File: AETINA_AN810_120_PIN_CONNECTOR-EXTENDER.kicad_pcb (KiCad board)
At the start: 2 copper layers, 86.5 x 20 mm, 4 parts, among them J1 QTH-060-01-X-D-A, J2 QSH-060-01-X-D-A

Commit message: Routing completed
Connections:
- J1 pad 01: Net-(J1-Pad01) -> /DSI3_D1_N
- J1 pad 02: Net-(J1-Pad02) -> /VDD_SYS_BL
- J1 pad 03: Net-(J1-Pad03) -> /DSI3_D1_P
- J1 pad 04: Net-(J1-Pad04) -> /VDD_SYS_BL
- J1 pad 05: Net-(J1-Pad05) -> GND
- J1 pad 06: Net-(J1-Pad06) -> /VDD_SYS_BL
- J1 pad 07: Net-(J1-Pad07) -> /DSI3_D0_N
- J1 pad 08: Net-(J1-Pad08) -> /LCD_BKLT_EN
- J1 pad 09: Net-(J1-Pad09) -> /DSI3_D0_P
- J1 pad 10: Net-(J1-Pad10) -> /LCD_BKLT0_PWM
- J1 pad 100: (no net) -> /LCD_BKLT1_PWM
- J1 pad 101: (no net) -> /DP0_TX1_N
- J1 pad 102: (no net) -> GND
- J1 pad 103: (no net) -> GND
- J1 pad 104: (no net) -> /SPI2_SCK
- J1 pad 105: (no net) -> /DP0_TX2_P
- J1 pad 106: (no net) -> /SPI2_MISO
- J1 pad 107: (no net) -> /DP0_TX2_N
- J1 pad 108: (no net) -> /SPI2_MOSI
- J1 pad 109: (no net) -> GND
- J1 pad 11: Net-(J1-Pad11) -> GND
- J1 pad 110: (no net) -> /SPI2_CS0
- J1 pad 111: (no net) -> Net-(J1-Pad111)
- J1 pad 112: (no net) -> GND
- J1 pad 113: (no net) -> Net-(J1-Pad113)
- J1 pad 114: (no net) -> Net-(J1-Pad114)
- J1 pad 115: (no net) -> GND
- J1 pad 116: (no net) -> Net-(J1-Pad116)
- J1 pad 117: (no net) -> /DP0_TX3_P
- J1 pad 118: (no net) -> Net-(J1-Pad118)
- J1 pad 119: (no net) -> /DP0_TX3_N
- J1 pad 12: Net-(J1-Pad12) -> /LCD_EN
- J1 pad 120: (no net) -> Net-(J1-Pad120)
- J1 pad 13: Net-(J1-Pad13) -> /DSI3_CLK_N
- J1 pad 14: Net-(J1-Pad14) -> /LCD_TE
- J1 pad 15: Net-(J1-Pad15) -> /DSI3_CLK_P
- J1 pad 16: Net-(J1-Pad16) -> /VDD_3V3_SLP
- J1 pad 17: Net-(J1-Pad17) -> GND
- J1 pad 18: Net-(J1-Pad18) -> /BRIDGE_EN
- J1 pad 19: Net-(J1-Pad19) -> /DSI2_D1_N
- J1 pad 20: Net-(J1-Pad20) -> /BRIDGE_IRQ
- J1 pad 21: Net-(J1-Pad21) -> /DSI2_D1_P
- J1 pad 22: Net-(J1-Pad22) -> /I2C_GP0_CLK
- J1 pad 23: Net-(J1-Pad23) -> GND
- J1 pad 24: Net-(J1-Pad24) -> /I2C_GP0_DAT
- J1 pad 25: Net-(J1-Pad25) -> /DSI2_D0_N
- J1 pad 26: Net-(J1-Pad26) -> /AVDD_TS_DIS
- J1 pad 27: Net-(J1-Pad27) -> /DSI2_D0_P
- J1 pad 28: Net-(J1-Pad28) -> /VDD_TS_1V8
- J1 pad 29: Net-(J1-Pad29) -> GND
- J1 pad 30: Net-(J1-Pad30) -> /I2C_GP1_CLK
- J1 pad 31: Net-(J1-Pad31) -> /DSI1_D1_N
- J1 pad 32: Net-(J1-Pad32) -> /I2C_GP1_DAT
- J1 pad 33: Net-(J1-Pad33) -> /DSI1_D1_P
- J1 pad 35: Net-(J1-Pad35) -> GND
- J1 pad 37: Net-(J1-Pad37) -> /DSI1_D0_N
- J1 pad 39: Net-(J1-Pad39) -> /DSI1_D0_P
- J1 pad 41: Net-(J1-Pad41) -> GND
- J1 pad 43: Net-(J1-Pad43) -> /DSI0_CLK_N
- J1 pad 45: Net-(J1-Pad45) -> /DSI0_CLK_P
- J1 pad 47: Net-(J1-Pad47) -> GND
- J1 pad 48: Net-(J1-Pad48) -> GND
- J1 pad 49: Net-(J1-Pad49) -> /DSI0_D1_N
- J1 pad 51: Net-(J1-Pad51) -> /DSI0_D1_P
- J1 pad 52: Net-(J1-Pad52) -> GND
- J1 pad 53: Net-(J1-Pad53) -> GND
- J1 pad 54: Net-(J1-Pad54) -> /VDD_DIS_3V3_LCD
- J1 pad 55: Net-(J1-Pad55) -> /DSI0_D0_N
- J1 pad 56: Net-(J1-Pad56) -> /VDD_DIS_3V3_LCD
- J1 pad 57: Net-(J1-Pad57) -> /DSI0_D0_P
- J1 pad 58: Net-(J1-Pad58) -> /VDD_LCD_1V8_DIS
- J1 pad 59: Net-(J1-Pad59) -> GND
- J1 pad 60: Net-(J1-Pad60) -> GND
- J1 pad 61: (no net) -> /VDD_3V3_SYS
- J1 pad 62: (no net) -> /LCD_VDD_EN
- J1 pad 63: (no net) -> /VDD_3V3_SYS
- J1 pad 64: (no net) -> Net-(J1-Pad64)
- J1 pad 65: (no net) -> GND
- J1 pad 66: (no net) -> /DSI1_CLK_P
- J1 pad 67: (no net) -> GND
- J1 pad 68: (no net) -> /DSI1_CLK_N
- J1 pad 69: (no net) -> /VDD_1V8
- J1 pad 70: (no net) -> GND
- J1 pad 71: (no net) -> /VDD_1V8
- J1 pad 72: (no net) -> /DSI2_CLK_P
- J1 pad 73: (no net) -> GND
- J1 pad 74: (no net) -> /DSI2_CLK_N
- J1 pad 75: (no net) -> GND
- J1 pad 76: (no net) -> GND
- J1 pad 77: (no net) -> /VDD_1V2
- J1 pad 78: (no net) -> GND
- J1 pad 79: (no net) -> /VDD_1V2
- J1 pad 80: (no net) -> /VDD_5V0_IO_SYS
- J1 pad 81: (no net) -> GND
- J1 pad 82: (no net) -> Net-(J1-Pad82)
- J1 pad 83: (no net) -> GND
- J1 pad 84: (no net) -> Net-(J1-Pad84)
- J1 pad 85: (no net) -> /DP_HPD
- J1 pad 86: (no net) -> /CHARGER_PRSNT
- J1 pad 87: (no net) -> /DP0_AUX_CH_N
- J1 pad 88: (no net) -> /LCD_BIAS_EN
- J1 pad 89: (no net) -> /DP0_AUX_CH_P
- J1 pad 90: (no net) -> GND
- J1 pad 91: (no net) -> GND
- J1 pad 92: (no net) -> /GSYNC_VSYNC
- J1 pad 93: (no net) -> /DP0_TX0_P
- J1 pad 94: (no net) -> /GSYNC_HSYNC
- J1 pad 95: (no net) -> /DP0_TX0_N
- J1 pad 96: (no net) -> GND
- J1 pad 97: (no net) -> GND
- J1 pad 98: (no net) -> /NVSR_INT
- J1 pad 99: (no net) -> /DP0_TX1_P
- J1 pad G1: Net-(J1-PadG1) -> GND
- J1 pad G2: Net-(J1-PadG1) -> GND
- J1 pad G3: Net-(J1-PadG1) -> GND
- J1 pad G4: Net-(J1-PadG1) -> GND
- J1 pad G5: Net-(J1-PadG1) -> GND
- J1 pad G6: Net-(J1-PadG1) -> GND
- J1 pad G7: Net-(J1-PadG1) -> GND
- J1 pad G8: Net-(J1-PadG1) -> GND
- J2 pad 01: Net-(J2-Pad01) -> /DSI3_D1_N
- J2 pad 02: Net-(J2-Pad02) -> /VDD_SYS_BL
- J2 pad 03: Net-(J2-Pad03) -> /DSI3_D1_P
- J2 pad 04: Net-(J2-Pad04) -> /VDD_SYS_BL
- J2 pad 05: Net-(J2-Pad05) -> GND
- J2 pad 06: Net-(J2-Pad06) -> /VDD_SYS_BL
- J2 pad 07: Net-(J2-Pad07) -> /DSI3_D0_N
- J2 pad 08: Net-(J2-Pad08) -> /LCD_BKLT_EN
- J2 pad 09: Net-(J2-Pad09) -> /DSI3_D0_P
- J2 pad 10: Net-(J2-Pad10) -> /LCD_BKLT0_PWM
- J2 pad 100: (no net) -> /LCD_BKLT1_PWM
- J2 pad 101: (no net) -> /DP0_TX1_N
- J2 pad 102: (no net) -> GND
- J2 pad 103: (no net) -> GND
- J2 pad 104: (no net) -> /SPI2_SCK
- J2 pad 105: (no net) -> /DP0_TX2_P
- J2 pad 106: (no net) -> /SPI2_MISO
- J2 pad 107: (no net) -> /DP0_TX2_N
- J2 pad 108: (no net) -> /SPI2_MOSI
- J2 pad 109: (no net) -> GND
- J2 pad 11: Net-(J2-Pad11) -> GND
- J2 pad 110: (no net) -> /SPI2_CS0
- J2 pad 111: (no net) -> Net-(J2-Pad111)
- J2 pad 112: (no net) -> GND
- J2 pad 113: (no net) -> Net-(J2-Pad113)
- J2 pad 114: (no net) -> Net-(J2-Pad114)
- J2 pad 115: (no net) -> GND
- J2 pad 116: (no net) -> Net-(J2-Pad116)
- J2 pad 117: (no net) -> /DP0_TX3_P
- J2 pad 118: (no net) -> Net-(J2-Pad118)
- J2 pad 119: (no net) -> /DP0_TX3_N
- J2 pad 12: Net-(J2-Pad12) -> /LCD_EN
- J2 pad 120: (no net) -> Net-(J2-Pad120)
- J2 pad 13: Net-(J2-Pad13) -> /DSI3_CLK_N
- J2 pad 14: Net-(J2-Pad14) -> /LCD_TE
- J2 pad 15: Net-(J2-Pad15) -> /DSI3_CLK_P
- J2 pad 16: Net-(J2-Pad16) -> /VDD_3V3_SLP
- J2 pad 17: Net-(J2-Pad17) -> GND
- J2 pad 18: Net-(J2-Pad18) -> /BRIDGE_EN
- J2 pad 19: Net-(J2-Pad19) -> /DSI2_D1_N
- J2 pad 20: Net-(J2-Pad20) -> /BRIDGE_IRQ
- J2 pad 21: Net-(J2-Pad21) -> /DSI2_D1_P
- J2 pad 22: Net-(J2-Pad22) -> /I2C_GP0_CLK
- J2 pad 23: Net-(J2-Pad23) -> GND
- J2 pad 24: Net-(J2-Pad24) -> /I2C_GP0_DAT
- J2 pad 25: Net-(J2-Pad25) -> /DSI2_D0_N
- J2 pad 26: Net-(J2-Pad26) -> /AVDD_TS_DIS
- J2 pad 27: Net-(J2-Pad27) -> /DSI2_D0_P
- J2 pad 28: Net-(J2-Pad28) -> /VDD_TS_1V8
- J2 pad 29: Net-(J2-Pad29) -> GND
- J2 pad 30: Net-(J2-Pad30) -> /I2C_GP1_CLK
- J2 pad 31: Net-(J2-Pad31) -> /DSI1_D1_N
- J2 pad 32: Net-(J2-Pad32) -> /I2C_GP1_DAT
- J2 pad 33: Net-(J2-Pad33) -> /DSI1_D1_P
- J2 pad 35: Net-(J2-Pad35) -> GND
- J2 pad 37: Net-(J2-Pad37) -> /DSI1_D0_N
- J2 pad 39: Net-(J2-Pad39) -> /DSI1_D0_P
- J2 pad 41: Net-(J2-Pad41) -> GND
- J2 pad 43: Net-(J2-Pad43) -> /DSI0_CLK_N
- J2 pad 45: Net-(J2-Pad45) -> /DSI0_CLK_P
- J2 pad 47: Net-(J2-Pad47) -> GND
- J2 pad 48: Net-(J2-Pad48) -> GND
- J2 pad 49: Net-(J2-Pad49) -> /DSI0_D1_N
- J2 pad 51: Net-(J2-Pad51) -> /DSI0_D1_P
- J2 pad 52: Net-(J2-Pad52) -> GND
- J2 pad 53: Net-(J2-Pad53) -> GND
- J2 pad 54: Net-(J2-Pad54) -> /VDD_DIS_3V3_LCD
- J2 pad 55: Net-(J2-Pad55) -> /DSI0_D0_N
- J2 pad 56: Net-(J2-Pad56) -> /VDD_DIS_3V3_LCD
- J2 pad 57: Net-(J2-Pad57) -> /DSI0_D0_P
- J2 pad 58: Net-(J2-Pad58) -> /VDD_LCD_1V8_DIS
- J2 pad 59: Net-(J2-Pad59) -> GND
- J2 pad 60: Net-(J2-Pad60) -> GND
- J2 pad 61: (no net) -> /VDD_3V3_SYS
- J2 pad 62: (no net) -> /LCD_VDD_EN
- J2 pad 63: (no net) -> /VDD_3V3_SYS
- J2 pad 64: (no net) -> Net-(J2-Pad64)
- J2 pad 65: (no net) -> GND
- J2 pad 66: (no net) -> /DSI1_CLK_P
- J2 pad 67: (no net) -> GND
- J2 pad 68: (no net) -> /DSI1_CLK_N
- J2 pad 69: (no net) -> /VDD_1V8
- J2 pad 70: (no net) -> GND
- J2 pad 71: (no net) -> /VDD_1V8
- J2 pad 72: (no net) -> /DSI2_CLK_P
- J2 pad 73: (no net) -> GND
- J2 pad 74: (no net) -> /DSI2_CLK_N
- J2 pad 75: (no net) -> GND
- J2 pad 76: (no net) -> GND
- J2 pad 77: (no net) -> /VDD_1V2
- J2 pad 78: (no net) -> GND
- J2 pad 79: (no net) -> /VDD_1V2
- J2 pad 80: (no net) -> /VDD_5V0_IO_SYS
- J2 pad 81: (no net) -> GND
- J2 pad 82: (no net) -> Net-(J2-Pad82)
- J2 pad 83: (no net) -> GND
- J2 pad 84: (no net) -> Net-(J2-Pad84)
- J2 pad 85: (no net) -> /DP_HPD
- J2 pad 86: (no net) -> /CHARGER_PRSNT
- J2 pad 87: (no net) -> /DP0_AUX_CH_N
- J2 pad 88: (no net) -> /LCD_BIAS_EN
- J2 pad 89: (no net) -> /DP0_AUX_CH_P
- J2 pad 90: (no net) -> GND
- J2 pad 91: (no net) -> GND
- J2 pad 92: (no net) -> /GSYNC_VSYNC
- J2 pad 93: (no net) -> /DP0_TX0_P
- J2 pad 94: (no net) -> /GSYNC_HSYNC
- J2 pad 95: (no net) -> /DP0_TX0_N
- J2 pad 96: (no net) -> GND
- J2 pad 97: (no net) -> GND
- J2 pad 98: (no net) -> /NVSR_INT
- J2 pad 99: (no net) -> /DP0_TX1_P
- J2 pad G1_1: Net-(J2-PadG1_1) -> GND
- J2 pad G1_2: Net-(J2-PadG1_1) -> GND
- J2 pad G1_3: Net-(J2-PadG1_1) -> GND
- J2 pad G1_4: Net-(J2-PadG1_1) -> GND
- J2 pad G2_1: (no net) -> GND
- J2 pad G2_2: (no net) -> GND
- J2 pad G2_3: (no net) -> GND
- J2 pad G2_4: (no net) -> GND
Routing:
- net GND: track 0.00 -> 259.3 mm, vias 0 -> 11
- net /VDD_SYS_BL: track 0.00 -> 21.4 mm, vias 0 -> 1
- net /VDD_1V2: track 0.00 -> 16.1 mm, vias 0 -> 1
- net /VDD_1V8: track 0.00 -> 15.7 mm, vias 0 -> 1
- net /I2C_GP1_DAT: track 0.00 -> 15.6 mm, vias 0 -> 1
- net /VDD_DIS_3V3_LCD: track 0.00 -> 15.5 mm, vias 0 -> 1
- net /VDD_3V3_SYS: track 0.00 -> 15.3 mm, vias 0 -> 1
- net /I2C_GP1_CLK: track 0.00 -> 15.2 mm, vias 0 -> 1
- net /DSI0_D0_P: track 0.00 -> 14.9 mm, vias 0 -> 1
- net /DSI0_D0_N: track 0.00 -> 14.4 mm, vias 0 -> 1
- net /DSI0_D1_P: track 0.00 -> 13.7 mm, vias 0 -> 1
- net /VDD_TS_1V8: track 0.00 -> 13.6 mm, vias 0 -> 1
- net /DSI0_CLK_P: track 0.00 -> 13.0 mm, vias 0 -> 1
- net /DSI0_D1_N: track 0.00 -> 13.0 mm, vias 0 -> 1
- net /DSI1_D0_P: track 0.00 -> 12.6 mm, vias 0 -> 1
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- added copper zone on B.Cu, net GND
- added copper zone on F.Cu, net GND

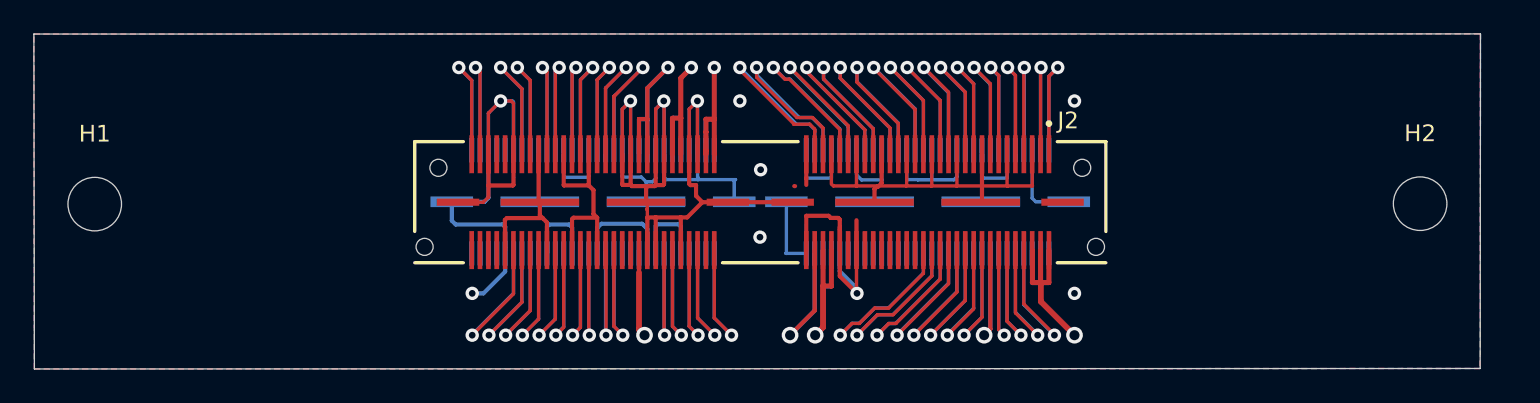
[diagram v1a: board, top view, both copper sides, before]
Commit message: Fix wrong wiring by referring to incorrect connector
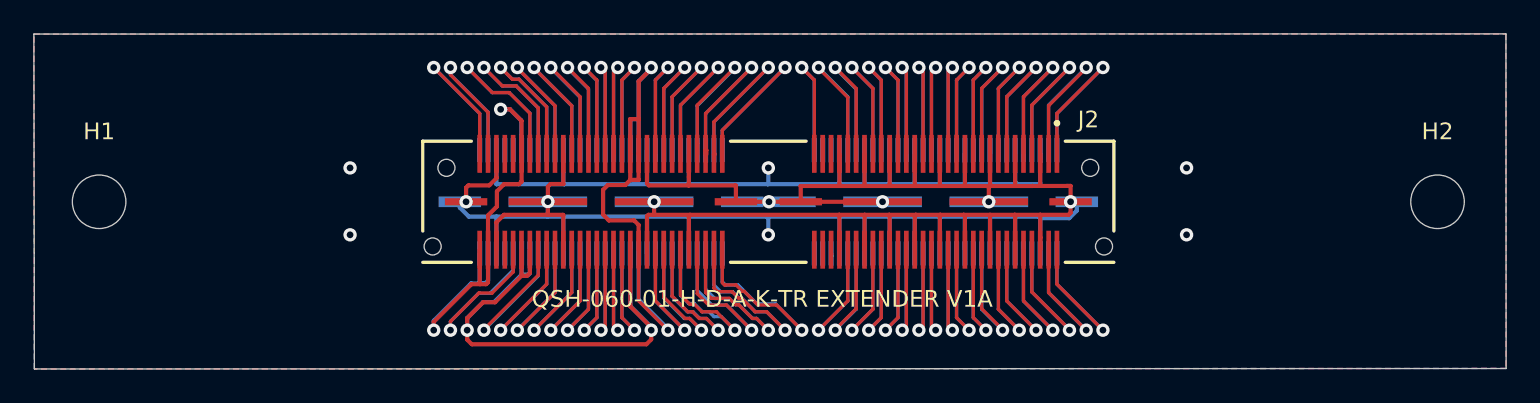
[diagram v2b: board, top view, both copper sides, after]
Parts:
- moved H2 1.05 mm to (210.7, 100.0)
- moved J2 0.48 mm to (170.7, 100.0)
- moved J1 0.48 mm to (170.7, 100.0)
- moved H1 0.30 mm to (130.7, 100.0)
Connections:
- net /AVDD_TS_DIS renamed /CSI_D_CLK_P
- net /BRIDGE_IRQ renamed /CSI_D_D0_P
- net /CHARGER_PRSNT renamed /CAM_VSYNC
- net /DP0_AUX_CH_N renamed /I2C_PM_CLK
- net /DP0_AUX_CH_P renamed /I2C_PM_DAT
- net /DP0_TX0_N renamed /CAM0_RST_L
- net /DP0_TX0_P renamed /CAM0_PWDN
- net /DP0_TX1_N renamed /DVDD_CAM_IO_1V2
- net /DP0_TX2_N renamed /I2C_GP0_DAT_1V8
- net /DP0_TX2_P renamed /I2C_GP0_CLK_1V8
- net /DP0_TX3_N renamed /VDD_SYS_EN
- net /DP0_TX3_P renamed /MDM2AP_READY_1V8
- net /DP_HPD renamed /CAM_AF_PWDN
- net /DSI0_CLK_N renamed /CSI_E_CLK_P
- net /DSI0_CLK_P renamed /CSI_E_CLK_N
- net /DSI0_D1_N renamed /CSI_E_D1_P
- net /DSI0_D1_P renamed /CSI_E_D1_N
- net /DSI1_CLK_P renamed /SPI2_CS1
- net /DSI1_D0_N renamed /CSI_E_D0_P
- net /DSI1_D0_P renamed /CSI_E_D0_N
- net /DSI1_D1_N renamed /CSI_C_D1_P
- net /DSI1_D1_P renamed /CSI_C_D1_N
- net /DSI2_CLK_N renamed /I2S3_LRCLK
- net /DSI2_CLK_P renamed /I2S3_CLK
- net /DSI2_D0_N renamed /CSI_C_CLK_P
- net /DSI2_D0_P renamed /CSI_C_CLK_N
- net /DSI2_D1_N renamed /CSI_C_D0_P
- net /DSI2_D1_P renamed /CSI_C_D0_N
- net /DSI3_CLK_N renamed /CSI_A_D1_P
- net /DSI3_CLK_P renamed /CSI_A_D1_N
- net /DSI3_D0_N renamed /CSI_A_CLK_P
- net /DSI3_D0_P renamed /CSI_A_CLK_N
- net /DSI3_D1_N renamed /CSI_A_D0_P
- net /DSI3_D1_P renamed /CSI_A_D0_N
- net /GSYNC_HSYNC renamed /CAM2_MCLK
- net /GSYNC_VSYNC renamed /CAM1_RST_L
- net /I2C_GP0_CLK renamed /CSI_D_D0_N
- net /I2C_GP1_DAT renamed /CSI_D_D1_P
- net /LCD_BIAS_EN renamed /CAM1_MCLK
- net /LCD_BKLT0_PWM renamed /CSI_B_CLK_N
- net /LCD_BKLT_EN renamed /CSI_B_CLK_P
- net /LCD_TE renamed /CSI_B_D1_P
- net /NVSR_INT renamed /CAM2_RST
- net /VDD_TS_1V8 renamed /CSI_D_CLK_N
- J1 pad 02: /VDD_SYS_BL -> /CSI_B_D0_P
- J1 pad 04: /VDD_SYS_BL -> /CSI_B_D0_N
- J1 pad 06: /VDD_SYS_BL -> GND
- J1 pad 100: /LCD_BKLT1_PWM -> GND
- J1 pad 102: GND -> /DVDD_CAM_IO_1V8
- J1 pad 103: GND -> /FLASH_INHIBIT
- J1 pad 104: /SPI2_SCK -> /TORCH_EN
- J1 pad 106: /SPI2_MISO -> /FLASH_STROBE
- J1 pad 108: /SPI2_MOSI -> /VDD_3V3_SLP
- J1 pad 109: GND -> /VDD_5V0_IO_SYS
- J1 pad 110: /SPI2_CS0 -> /VDD_3V3_SLP
- J1 pad 112: GND -> /MOTION_INT_AP_L
- J1 pad 116: Net-(J1-Pad116) -> GND
- J1 pad 118: Net-(J1-Pad118) -> /VDD_5V0_IO_SYS
- J1 pad 12: /LCD_EN -> GND
- J1 pad 120: Net-(J1-Pad120) -> /VDD_5V0_IO_SYS
- J1 pad 16: /VDD_3V3_SLP -> /CSI_B_D1_N
- J1 pad 18: /BRIDGE_EN -> GND
- J1 pad 24: /I2C_GP0_DAT -> GND
- J1 pad 30: /I2C_GP1_CLK -> GND
- J1 pad 34: Net-(J1-Pad34) -> /CSI_D_D1_N
- J1 pad 36: Net-(J1-Pad36) -> GND
- J1 pad 38: Net-(J1-Pad38) -> /CSI_F_D0_P
- J1 pad 40: Net-(J1-Pad40) -> /CSI_F_D0_N
- J1 pad 42: Net-(J1-Pad42) -> GND
- J1 pad 44: Net-(J1-Pad44) -> /CSI_F_CLK_P
- J1 pad 46: Net-(J1-Pad46) -> /CSI_F_CLK_N
- J1 pad 50: Net-(J1-Pad50) -> /CSI_F_D1_P
- J1 pad 52: GND -> /CSI_F_D1_N
- J1 pad 54: /VDD_DIS_3V3_LCD -> GND
- J1 pad 55: /DSI0_D0_N -> Net-(J1-Pad55)
- J1 pad 56: /VDD_DIS_3V3_LCD -> Net-(J1-Pad56)
- J1 pad 57: /DSI0_D0_P -> Net-(J1-Pad57)
- J1 pad 58: /VDD_LCD_1V8_DIS -> Net-(J1-Pad58)
- J1 pad 59: GND -> /CAM_UART3_PSNT_L
- J1 pad 60: GND -> Net-(J1-Pad60)
- J1 pad 61: /VDD_3V3_SYS -> /CAM_UART3_TXD
- J1 pad 62: /LCD_VDD_EN -> /SPI2_SCK
- J1 pad 63: /VDD_3V3_SYS -> /CAM_UART3_RXD
- J1 pad 64: Net-(J1-Pad64) -> /SPI2_MISO
- J1 pad 65: GND -> /CAM_UART3_CTS
- J1 pad 67: GND -> /CAM_UART3_RTS
- J1 pad 68: /DSI1_CLK_N -> /SPI2_MOSI
- J1 pad 69: /VDD_1V8 -> GND
- J1 pad 71: /VDD_1V8 -> /AO_DMIC_IN_CLK
- J1 pad 73: GND -> /AO_DMIC_IN_DAT
- J1 pad 75: GND -> /CAM_I2C_SCL
- J1 pad 76: GND -> /I2S3_SDIN
- J1 pad 77: /VDD_1V2 -> /CAM_I2C_SDA
- J1 pad 78: GND -> /I2S3_SDOUT
- J1 pad 79: /VDD_1V2 -> GND
- J1 pad 80: /VDD_5V0_IO_SYS -> GND
- J1 pad 81: GND -> /AVDD_CAM
- J1 pad 82: Net-(J1-Pad82) -> /AVDD_CAM
- J1 pad 83: GND -> /AVDD_CAM
- J1 pad 84: Net-(J1-Pad84) -> /VDD_3V3_SLP
- J1 pad 90: GND -> /CAM1_PWDN
- J1 pad 91: GND -> /CAM0_MCLK
- J1 pad 96: GND -> /CAM2_PWDN
- J1 pad 97: GND -> /FLASH_EN
- J1 pad 99: /DP0_TX1_P -> GND
- J2 pad 02: /VDD_SYS_BL -> /CSI_B_D0_P
- J2 pad 04: /VDD_SYS_BL -> /CSI_B_D0_N
- J2 pad 06: /VDD_SYS_BL -> GND
- J2 pad 100: /LCD_BKLT1_PWM -> GND
- J2 pad 102: GND -> /DVDD_CAM_IO_1V8
- J2 pad 103: GND -> /FLASH_INHIBIT
- J2 pad 104: /SPI2_SCK -> /TORCH_EN
- J2 pad 106: /SPI2_MISO -> /FLASH_STROBE
- J2 pad 108: /SPI2_MOSI -> /VDD_3V3_SLP
- J2 pad 109: GND -> /VDD_5V0_IO_SYS
- J2 pad 110: /SPI2_CS0 -> /VDD_3V3_SLP
- J2 pad 112: GND -> /MOTION_INT_AP_L
- J2 pad 116: Net-(J2-Pad116) -> GND
- J2 pad 118: Net-(J2-Pad118) -> /VDD_5V0_IO_SYS
- J2 pad 12: /LCD_EN -> GND
- J2 pad 120: Net-(J2-Pad120) -> /VDD_5V0_IO_SYS
- J2 pad 16: /VDD_3V3_SLP -> /CSI_B_D1_N
- J2 pad 18: /BRIDGE_EN -> GND
- J2 pad 24: /I2C_GP0_DAT -> GND
- J2 pad 30: /I2C_GP1_CLK -> GND
- J2 pad 34: Net-(J2-Pad34) -> /CSI_D_D1_N
- J2 pad 36: Net-(J2-Pad36) -> GND
- J2 pad 38: Net-(J2-Pad38) -> /CSI_F_D0_P
- J2 pad 40: Net-(J2-Pad40) -> /CSI_F_D0_N
- J2 pad 42: Net-(J2-Pad42) -> GND
- J2 pad 44: Net-(J2-Pad44) -> /CSI_F_CLK_P
- J2 pad 46: Net-(J2-Pad46) -> /CSI_F_CLK_N
- J2 pad 50: Net-(J2-Pad50) -> /CSI_F_D1_P
- J2 pad 52: GND -> /CSI_F_D1_N
- J2 pad 54: /VDD_DIS_3V3_LCD -> GND
- J2 pad 55: /DSI0_D0_N -> Net-(J2-Pad55)
- J2 pad 56: /VDD_DIS_3V3_LCD -> Net-(J2-Pad56)
- J2 pad 57: /DSI0_D0_P -> Net-(J2-Pad57)
- J2 pad 58: /VDD_LCD_1V8_DIS -> Net-(J2-Pad58)
- J2 pad 59: GND -> /CAM_UART3_PSNT_L
- J2 pad 60: GND -> Net-(J2-Pad60)
- J2 pad 61: /VDD_3V3_SYS -> /CAM_UART3_TXD
- J2 pad 62: /LCD_VDD_EN -> /SPI2_SCK
- J2 pad 63: /VDD_3V3_SYS -> /CAM_UART3_RXD
- J2 pad 64: Net-(J2-Pad64) -> /SPI2_MISO
- J2 pad 65: GND -> /CAM_UART3_CTS
- J2 pad 67: GND -> /CAM_UART3_RTS
- J2 pad 68: /DSI1_CLK_N -> /SPI2_MOSI
- J2 pad 69: /VDD_1V8 -> GND
- J2 pad 71: /VDD_1V8 -> /AO_DMIC_IN_CLK
- J2 pad 73: GND -> /AO_DMIC_IN_DAT
- J2 pad 75: GND -> /CAM_I2C_SCL
- J2 pad 76: GND -> /I2S3_SDIN
- J2 pad 77: /VDD_1V2 -> /CAM_I2C_SDA
- J2 pad 78: GND -> /I2S3_SDOUT
- J2 pad 79: /VDD_1V2 -> GND
- J2 pad 80: /VDD_5V0_IO_SYS -> GND
- J2 pad 81: GND -> /AVDD_CAM
- J2 pad 82: Net-(J2-Pad82) -> /AVDD_CAM
- J2 pad 83: GND -> /AVDD_CAM
- J2 pad 84: Net-(J2-Pad84) -> /VDD_3V3_SLP
- J2 pad 90: GND -> /CAM1_PWDN
- J2 pad 91: GND -> /CAM0_MCLK
- J2 pad 96: GND -> /CAM2_PWDN
- J2 pad 97: GND -> /FLASH_EN
- J2 pad 99: /DP0_TX1_P -> GND
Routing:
- net /AVDD_CAM: track 0.00 -> 37.4 mm, vias 0 -> 2
- net /VDD_3V3_SLP: track 10.3 -> 39.4 mm, vias 1 -> 2
- net /VDD_SYS_BL: track 21.4 -> 0.00 mm, vias 1 -> 0
- net /VDD_5V0_IO_SYS: track 10.2 -> 31.1 mm, vias 1 -> 2
- net /VDD_1V2: track 16.1 -> 0.00 mm, vias 1 -> 0
- net /VDD_1V8: track 15.7 -> 0.00 mm, vias 1 -> 0
- net /VDD_DIS_3V3_LCD: track 15.5 -> 0.00 mm, vias 1 -> 0
- net /VDD_3V3_SYS: track 15.3 -> 0.00 mm, vias 1 -> 0
- net /I2C_GP1_CLK: track 15.2 -> 0.00 mm, vias 1 -> 0
- net /DSI0_D0_P: track 14.9 -> 0.00 mm, vias 1 -> 0
- net /DSI0_D0_N: track 14.4 -> 0.00 mm, vias 1 -> 0
- net /MOTION_INT_AP_L: track 0.00 -> 13.4 mm, vias 0 -> 1
- net /CAM_UART3_TXD: track 0.00 -> 13.2 mm, vias 0 -> 1
- net /CAM_UART3_CTS: track 0.00 -> 13.1 mm, vias 0 -> 1
- net /FLASH_INHIBIT: track 0.00 -> 12.8 mm, vias 0 -> 1
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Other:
- board size 86.5 x 20 mm -> 88 x 20 mm
